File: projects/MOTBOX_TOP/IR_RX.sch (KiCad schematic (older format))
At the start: 2 parts, among them J18 Conn_01x02

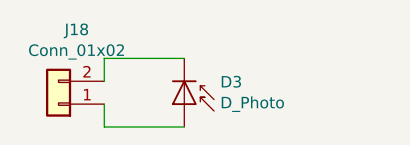
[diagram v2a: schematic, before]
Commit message: New library files and schematics with ESE31 and DT045 switches
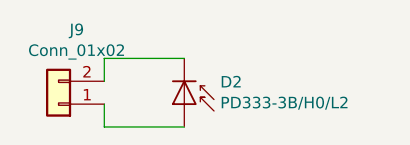
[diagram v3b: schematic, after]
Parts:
- D2: renamed from D3; value D_Photo -> PD333-3B/H0/L2
- renumbered J18 to J9
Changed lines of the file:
@@
 EESchema Schematic File Version 4
-LIBS:MOTBOX_TOP-cache
+LIBS:MOTBOX_TOP_ESE31-cache
 EELAYER 26 0
 EELAYER END
@@
 $EndDescr
 $Comp
-L Device:D_Photo D3
+L Device:D_Photo D2
 U 1 1 5CC07017
 P 5000 2500
-F 0 "D3" V 4904 2657 50  0000 L CNN
-F 1 "D_Photo" V 4995 2657 50  0000 L CNN
+F 0 "D2" V 4904 2657 50  0000 L CNN
+F 1 "PD333-3B/H0/L2" V 4995 2657 50  0000 L CNN
 F 2 "LED_THT:LED_D5.0mm_Horizontal_O6.35mm_Z9.0mm" H 4950 2500 50  0001 C CNN
 F 3 "~" H 4950 2500 50  0001 C CNN
@@
 	4650 2600 5000 2600
 $Comp
-L Connector_Generic:Conn_01x02 J18
+L Connector_Generic:Conn_01x02 J9
 U 1 1 5CC27F6C
 P 4450 2500
-F 0 "J18" H 4370 2175 50  0000 C CNN
+F 0 "J9" H 4370 2175 50  0000 C CNN
 F 1 "Conn_01x02" H 4370 2266 50  0000 C CNN
 F 2 "Connector_Wire:SolderWirePad_1x02_P3.81mm_Drill0.8mm" H 4450 2500 50  0001 C CNN
